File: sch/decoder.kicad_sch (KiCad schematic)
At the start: 3 parts

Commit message: Bus control
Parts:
- UA1: value (none) -> ~; footprint (none) -> Package_SO:SO-14_3.9x8.65mm_P1.27mm
- UDEC1: value (none) -> 74HC237; footprint (none) -> Package_SO:SOP-16_4.4x10.4mm_P1.27mm
- UI1: value (none) -> ~; footprint (none) -> Package_SO:SO-16_3.9x9.9mm_P1.27mm
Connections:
- net D0 renamed A21
- net D1 renamed A22
- net D2 renamed A23
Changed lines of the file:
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@@
     (effects (font (size 1.27 1.27)) (justify left bottom))
   )
-  (label "D2" (at 130.81 91.44 0)
-    (effects (font (size 1.27 1.27) bold) (justify left bottom))
-  )
-  (label "D[0..2]" (at 128.27 82.55 0)
-    (effects (font (size 1.27 1.27) bold) (justify left bottom))
-  )
-  (label "D1" (at 130.81 88.9 0)
-    (effects (font (size 1.27 1.27) bold) (justify left bottom))
-  )
-  (label "D0" (at 130.81 86.36 0)
-    (effects (font (size 1.27 1.27) bold) (justify left bottom))
+  (label "A23" (at 130.81 91.44 0)
+    (effects (font (size 1.27 1.27)) (justify left bottom))
+  )
+  (label "A22" (at 130.81 88.9 0)
+    (effects (font (size 1.27 1.27)) (justify left bottom))
+  )
+  (label "A[21..23]" (at 128.27 82.55 0)
+    (effects (font (size 1.27 1.27)) (justify left bottom))
+  )
+  (label "A21" (at 130.81 86.36 0)
+    (effects (font (size 1.27 1.27)) (justify left bottom))
   )
   (hierarchical_label "~{RAM0_EN}" (shape output) (at 213.36 88.9 0)
@@
     (effects (font (size 1.27 1.27)) (justify right))
   )
-  (hierarchical_label "MEM{D[0..7]}" (shape input) (at 128.27 78.74 90)
+  (hierarchical_label "A[0..23]" (shape input) (at 128.27 78.74 90)
     (effects (font (size 1.27 1.27)) (justify left))
   )
@@
     (in_bom yes) (on_board yes)
     (property "Reference" "UA1" (id 0) (at 171.45 74.93 0))
-    (property "Value" "" (id 1) (at 171.45 76.2 0))
-    (property "Footprint" "" (id 2) (at 171.45 74.93 0)
+    (property "Value" "~" (id 1) (at 171.45 76.2 0))
+    (property "Footprint" "Package_SO:SO-14_3.9x8.65mm_P1.27mm" (id 2) (at 171.45 74.93 0)
       (effects (font (size 1.27 1.27)) hide)
     )
@@
       (effects (font (size 1.27 1.27)) hide)
     )
-    (property "Value" "" (id 1) (at 140.97 80.01 0))
+    (property "Value" "~" (id 1) (at 140.97 80.01 0))
     (property "Footprint" "" (id 2) (at 144.78 81.28 0)
       (effects (font (size 1.27 1.27)) hide)
@@
       (effects (font (size 1.27 1.27)) hide)
     )
-    (property "Value" "" (id 1) (at 194.31 123.19 0))
+    (property "Value" "~" (id 1) (at 194.31 123.19 0))
     (property "Footprint" "" (id 2) (at 194.31 128.27 0)
       (effects (font (size 1.27 1.27)) hide)
@@
       (effects (font (size 1.27 1.27)) (justify left))
     )
-    (property "Value" "" (id 1) (at 146.7994 81.28 0)
+    (property "Value" "74HC237" (id 1) (at 146.7994 81.28 0)
       (effects (font (size 1.27 1.27)) (justify left))
     )
-    (property "Footprint" "" (id 2) (at 144.78 96.52 0)
+    (property "Footprint" "Package_SO:SOP-16_4.4x10.4mm_P1.27mm" (id 2) (at 144.78 96.52 0)
       (effects (font (size 1.27 1.27)) hide)
     )
@@
     (in_bom yes) (on_board yes)
     (property "Reference" "UI1" (id 0) (at 204.47 96.52 0))
-    (property "Value" "" (id 1) (at 205.74 90.17 0)
-      (effects (font (size 1.27 1.27)) hide)
-    )
-    (property "Footprint" "" (id 2) (at 205.74 96.52 0)
+    (property "Value" "~" (id 1) (at 205.74 90.17 0)
+      (effects (font (size 1.27 1.27)) hide)
+    )
+    (property "Footprint" "Package_SO:SO-16_3.9x9.9mm_P1.27mm" (id 2) (at 205.74 96.52 0)
       (effects (font (size 1.27 1.27)) hide)
     )
@@
     (in_bom yes) (on_board yes)
     (property "Reference" "UA1" (id 0) (at 104.14 90.17 0))
-    (property "Value" "" (id 1) (at 104.14 91.44 0))
-    (property "Footprint" "" (id 2) (at 104.14 90.17 0)
+    (property "Value" "~" (id 1) (at 104.14 91.44 0))
+    (property "Footprint" "Package_SO:SO-14_3.9x8.65mm_P1.27mm" (id 2) (at 104.14 90.17 0)
       (effects (font (size 1.27 1.27)) hide)
     )
@@
     (in_bom yes) (on_board yes)
     (property "Reference" "UI1" (id 0) (at 87.63 76.2 0))
-    (property "Value" "" (id 1) (at 88.9 69.85 0)
-      (effects (font (size 1.27 1.27)) hide)
-    )
-    (property "Footprint" "" (id 2) (at 88.9 76.2 0)
+    (property "Value" "~" (id 1) (at 88.9 69.85 0)
+      (effects (font (size 1.27 1.27)) hide)
+    )
+    (property "Footprint" "Package_SO:SO-16_3.9x9.9mm_P1.27mm" (id 2) (at 88.9 76.2 0)
       (effects (font (size 1.27 1.27)) hide)
     )
@@
       (effects (font (size 1.27 1.27)) hide)
     )
-    (property "Value" "" (id 1) (at 144.78 114.3 0))
+    (property "Value" "~" (id 1) (at 144.78 114.3 0))
     (property "Footprint" "" (id 2) (at 144.78 109.22 0)
       (effects (font (size 1.27 1.27)) hide)
@@
     (in_bom yes) (on_board yes)
     (property "Reference" "UI1" (id 0) (at 87.63 92.71 0))
-    (property "Value" "" (id 1) (at 88.9 100.33 0)
-      (effects (font (size 1.27 1.27)) hide)
-    )
-    (property "Footprint" "" (id 2) (at 88.9 92.71 0)
+    (property "Value" "~" (id 1) (at 88.9 100.33 0)
+      (effects (font (size 1.27 1.27)) hide)
+    )
+    (property "Footprint" "Package_SO:SO-16_3.9x9.9mm_P1.27mm" (id 2) (at 88.9 92.71 0)
       (effects (font (size 1.27 1.27)) hide)
     )
@@
     (in_bom yes) (on_board yes)
     (property "Reference" "UI1" (id 0) (at 207.01 128.27 90))
-    (property "Value" "" (id 1) (at 208.28 128.27 0))
-    (property "Footprint" "" (id 2) (at 207.01 128.27 0)
+    (property "Value" "~" (id 1) (at 208.28 128.27 0))
+    (property "Footprint" "Package_SO:SO-16_3.9x9.9mm_P1.27mm" (id 2) (at 207.01 128.27 0)
       (effects (font (size 1.27 1.27)) hide)
     )
@@
     (in_bom yes) (on_board yes)
     (property "Reference" "UI1" (id 0) (at 204.47 111.76 0))
-    (property "Value" "" (id 1) (at 205.74 105.41 0)
-      (effects (font (size 1.27 1.27)) hide)
-    )
-    (property "Footprint" "" (id 2) (at 205.74 111.76 0)
+    (property "Value" "~" (id 1) (at 205.74 105.41 0)
+      (effects (font (size 1.27 1.27)) hide)
+    )
+    (property "Footprint" "Package_SO:SO-16_3.9x9.9mm_P1.27mm" (id 2) (at 205.74 111.76 0)
       (effects (font (size 1.27 1.27)) hide)
     )
@@
     (in_bom yes) (on_board yes)
     (property "Reference" "UI1" (id 0) (at 204.47 104.14 0))
-    (property "Value" "" (id 1) (at 205.74 97.79 0)
-      (effects (font (size 1.27 1.27)) hide)
-    )
-    (property "Footprint" "" (id 2) (at 205.74 104.14 0)
+    (property "Value" "~" (id 1) (at 205.74 97.79 0)
+      (effects (font (size 1.27 1.27)) hide)
+    )
+    (property "Footprint" "Package_SO:SO-16_3.9x9.9mm_P1.27mm" (id 2) (at 205.74 104.14 0)
       (effects (font (size 1.27 1.27)) hide)
     )
@@
     (in_bom yes) (on_board yes)
     (property "Reference" "UI1" (id 0) (at 204.47 88.9 0))
-    (property "Value" "" (id 1) (at 205.74 82.55 0)
-      (effects (font (size 1.27 1.27)) hide)
-    )
-    (property "Footprint" "" (id 2) (at 205.74 88.9 0)
+    (property "Value" "~" (id 1) (at 205.74 82.55 0)
+      (effects (font (size 1.27 1.27)) hide)
+    )
+    (property "Footprint" "Package_SO:SO-16_3.9x9.9mm_P1.27mm" (id 2) (at 205.74 88.9 0)
       (effects (font (size 1.27 1.27)) hide)
     )
@@
       (effects (font (size 1.27 1.27)) hide)
     )
-    (property "Value" "" (id 1) (at 222.25 129.5399 0)
+    (property "Value" "~" (id 1) (at 222.25 129.5399 0)
       (effects (font (size 1.27 1.27)) (justify left))
     )

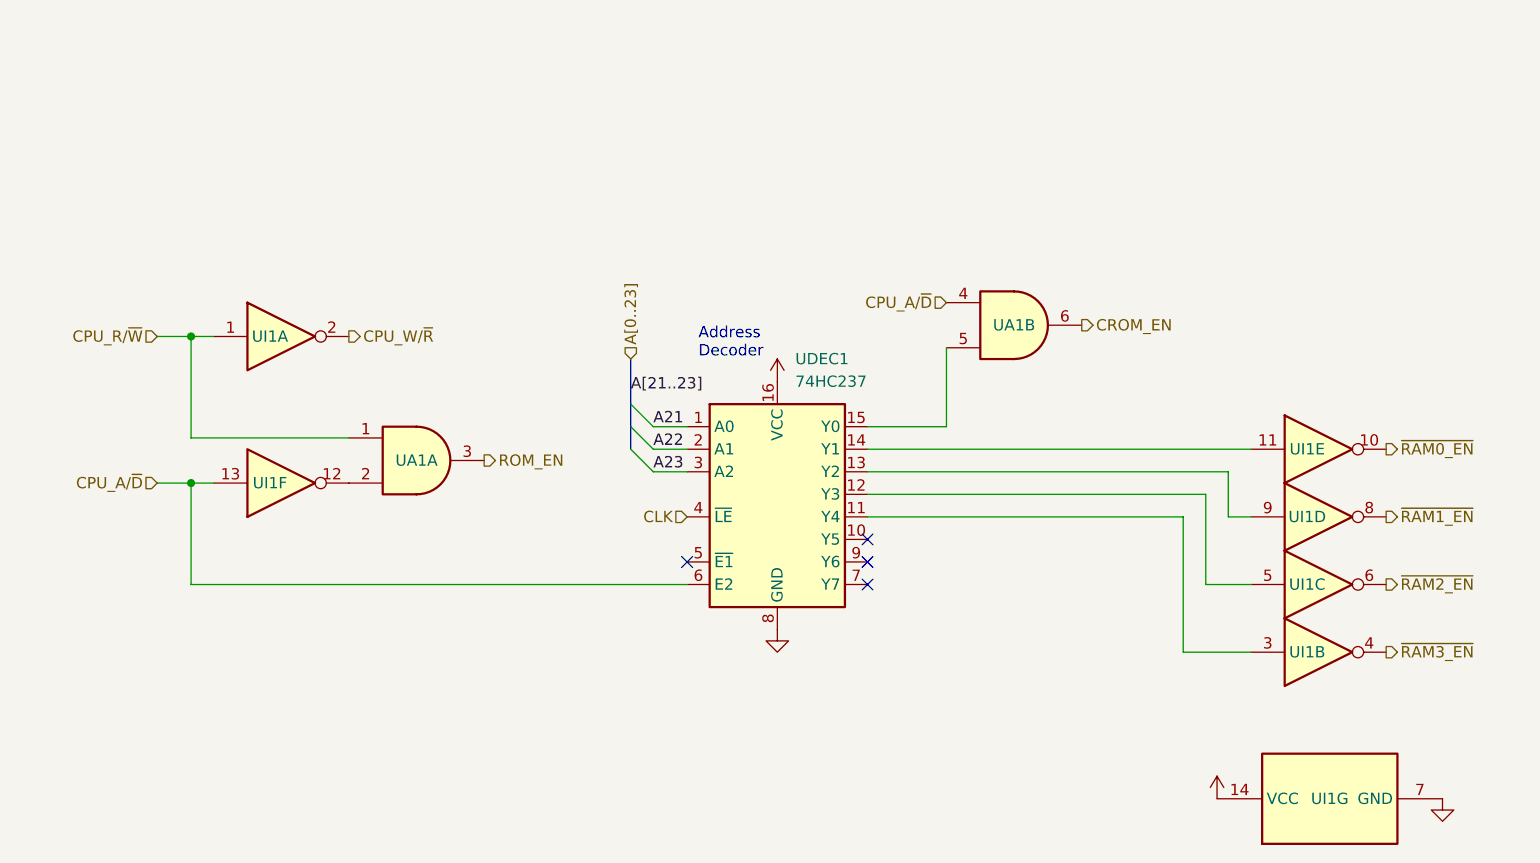
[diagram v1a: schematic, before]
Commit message: New address decoder
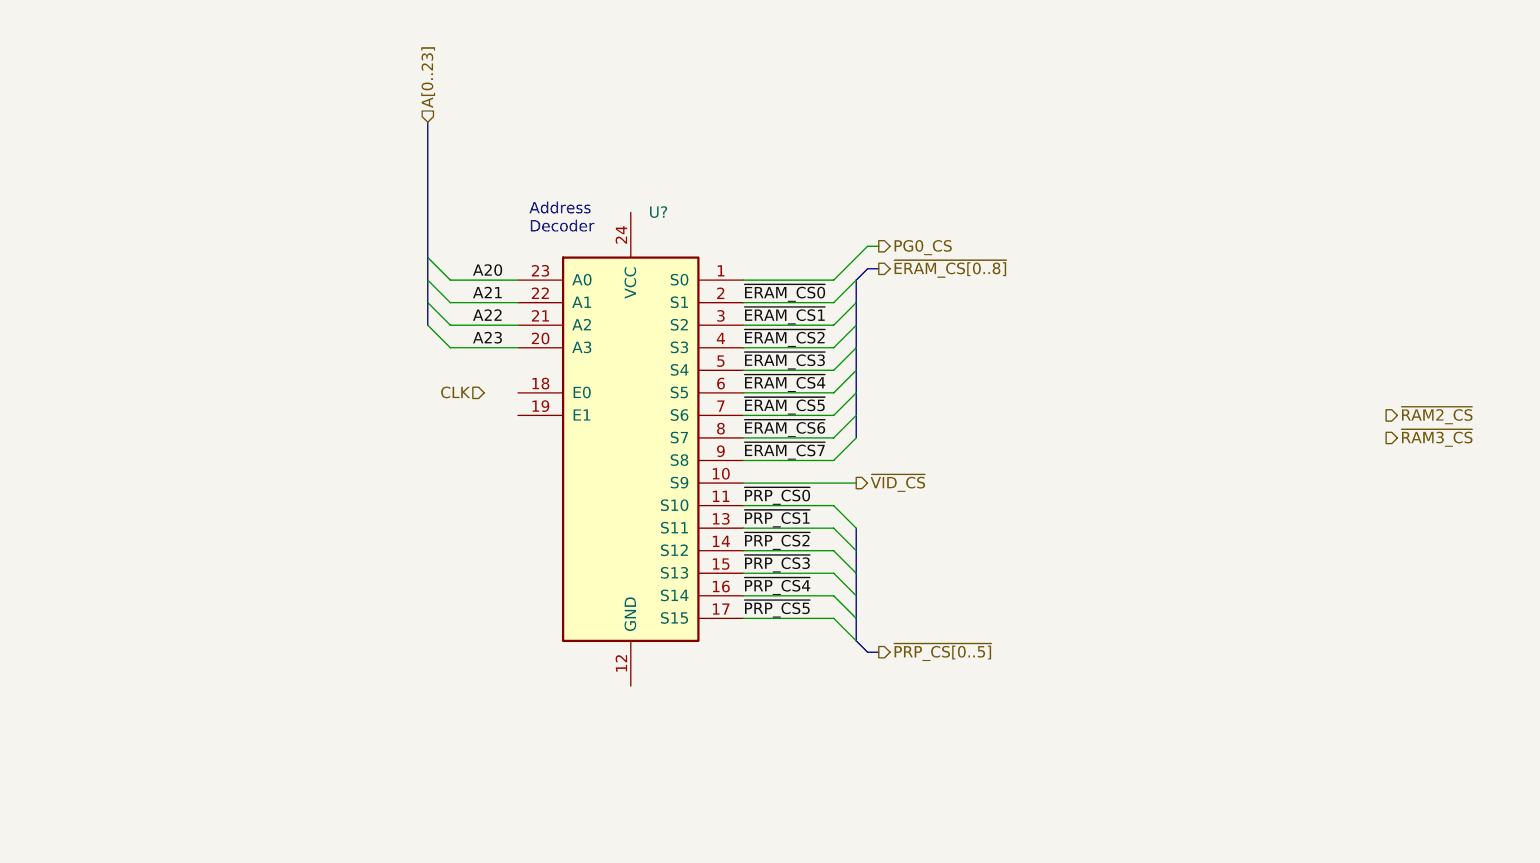
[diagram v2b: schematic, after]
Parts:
- removed UA1: ~, Package_SO:SO-14_3.9x8.65mm_P1.27mm, symbol 74xx:74LS08
- removed UDEC1: 74HC237, Package_SO:SOP-16_4.4x10.4mm_P1.27mm, symbol 74xx:74HC237
- removed UI1: ~, Package_SO:SO-16_3.9x9.9mm_P1.27mm, symbol 74xx:74HC04
- added U?: (no value), symbol 74xx:74LS154
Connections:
- net A21: now also U?.22 (A1)
- net A22: now also U?.21 (A2)
- net A23: now also U?.20 (A3)
- new net A20: U?.23 (A0)
- new net PG0_CS: U?.1 (S0)
- new net ~{ERAM_CS0}: U?.2 (S1)
- new net ~{ERAM_CS1}: U?.3 (S2)
- new net ~{ERAM_CS2}: U?.4 (S3)
- new net ~{ERAM_CS3}: U?.5 (S4)
- new net ~{ERAM_CS4}: U?.6 (S5)
- new net ~{ERAM_CS5}: U?.7 (S6)
- new net ~{ERAM_CS6}: U?.8 (S7)
- new net ~{ERAM_CS7}: U?.9 (S8)
- new net ~{PRP_CS0}: U?.11 (S10)
- new net ~{PRP_CS1}: U?.13 (S11)
- new net ~{PRP_CS2}: U?.14 (S12)
- new net ~{PRP_CS3}: U?.15 (S13)
- new net ~{PRP_CS4}: U?.16 (S14)
- new net ~{PRP_CS5}: U?.17 (S15)
- new net ~{VID_CS}: U?.10 (S9)
- no-connect marks 4 -> 0
